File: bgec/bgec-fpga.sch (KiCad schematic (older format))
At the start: 1 part

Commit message: Switch to better FPGA for routing
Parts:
- removed FPGAiCE40HX1: ICE40HX8K-CT256, bgec:BGA256C80P16X16_1400X1400X170, symbol bgec:ICE40HX8K-CT256
- added FPGAiCE40HX1: ICE40HX4K-TQ144, Package_QFP:TQFP-144_20x20mm_P0.5mm, symbol FPGA_Lattice:ICE40HX4K-TQ144
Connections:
- wire segments 65 -> 47
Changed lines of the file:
@@
 Comment4 ""
 $EndDescr
-Text GLabel 2000 1100 0    50   Input ~ 0
+Text GLabel 1500 900  0    50   Input ~ 0
 GCLogic
 Wire Wire Line
-	2000 1100 2100 1100
-Wire Wire Line
-	2100 1100 2100 1200
-Wire Wire Line
-	2100 1100 2200 1100
-Wire Wire Line
-	2200 1100 2200 1200
-Connection ~ 2100 1100
-Wire Wire Line
-	2200 1100 2300 1100
-Wire Wire Line
-	2300 1100 2300 1200
-Connection ~ 2200 1100
-Wire Wire Line
-	2300 1100 2400 1100
-Wire Wire Line
-	2400 1100 2400 1200
-Connection ~ 2300 1100
-Wire Wire Line
-	2400 1100 4100 1100
-Wire Wire Line
-	4100 1100 4100 1200
-Connection ~ 2400 1100
-Wire Wire Line
-	4100 1100 4200 1100
-Wire Wire Line
-	4200 1100 4200 1200
-Connection ~ 4100 1100
-Wire Wire Line
-	4200 1100 4300 1100
-Wire Wire Line
-	4300 1100 4300 1200
-Connection ~ 4200 1100
-Wire Wire Line
-	4300 1100 4400 1100
-Wire Wire Line
-	4400 1100 4400 1200
-Connection ~ 4300 1100
-Wire Wire Line
-	1500 5800 1400 5800
-Wire Wire Line
-	1400 5900 1500 5900
-Wire Wire Line
-	1500 6000 1400 6000
-Wire Wire Line
-	1400 6100 1500 6100
-Wire Wire Line
-	1500 6200 1400 6200
-Wire Wire Line
-	1400 6300 1500 6300
-Wire Wire Line
-	1400 5700 1500 5700
-Wire Wire Line
-	1500 5600 1400 5600
-Wire Wire Line
-	1400 5500 1500 5500
-Wire Wire Line
-	1400 5400 1500 5400
-Wire Wire Line
-	1400 5300 1500 5300
-Wire Wire Line
-	1400 5200 1500 5200
-Wire Wire Line
-	1400 5100 1500 5100
-Wire Wire Line
-	1400 5000 1500 5000
-Wire Wire Line
-	1400 4900 1500 4900
-Wire Wire Line
-	1400 4800 1500 4800
-Wire Wire Line
-	1400 4700 1500 4700
-Wire Wire Line
-	1400 4600 1500 4600
-Wire Wire Line
-	1400 4500 1500 4500
-Wire Wire Line
-	1500 4400 1400 4400
-Wire Wire Line
-	1400 4300 1500 4300
-Wire Wire Line
-	1500 4200 1400 4200
-Wire Wire Line
-	1500 3900 1400 3900
-Wire Wire Line
-	1400 3800 1500 3800
-Wire Wire Line
-	1500 3700 1400 3700
-Wire Wire Line
-	1400 3600 1500 3600
-Wire Wire Line
-	1500 3500 1400 3500
-Wire Wire Line
-	1400 3400 1500 3400
-Text GLabel 1400 6100 0    50   Input ~ 0
+	4000 3900 3900 3900
+Wire Wire Line
+	3900 4000 4000 4000
+Wire Wire Line
+	4000 4100 3900 4100
+Wire Wire Line
+	3900 4200 4000 4200
+Wire Wire Line
+	3900 3800 4000 3800
+Wire Wire Line
+	4000 3700 3900 3700
+Wire Wire Line
+	3900 3600 4000 3600
+Wire Wire Line
+	3900 3500 4000 3500
+Wire Wire Line
+	3900 3400 4000 3400
+Wire Wire Line
+	3900 3300 4000 3300
+Wire Wire Line
+	3900 2400 4000 2400
+Wire Wire Line
+	3900 2300 4000 2300
+Wire Wire Line
+	3900 2200 4000 2200
+Wire Wire Line
+	3900 2100 4000 2100
+Wire Wire Line
+	3900 2000 4000 2000
+Wire Wire Line
+	3900 1900 4000 1900
+Wire Wire Line
+	3900 1800 4000 1800
+Wire Wire Line
+	4000 1700 3900 1700
+Wire Wire Line
+	3900 1600 4000 1600
+Wire Wire Line
+	4000 1500 3900 1500
+Wire Wire Line
+	1500 4000 1400 4000
+Wire Wire Line
+	1400 3900 1500 3900
+Text GLabel 3900 4200 0    50   Input ~ 0
 TriggerRDB0
-Text GLabel 1400 6000 0    50   Input ~ 0
+Text GLabel 3900 4100 0    50   Input ~ 0
 TriggerRDB1
-Text GLabel 1400 5900 0    50   Input ~ 0
+Text GLabel 3900 4000 0    50   Input ~ 0
 TriggerRDB2
-Text GLabel 1400 5800 0    50   Input ~ 0
+Text GLabel 3900 3900 0    50   Input ~ 0
 TriggerRDB3
-Text GLabel 1400 5700 0    50   Input ~ 0
+Text GLabel 3900 3800 0    50   Input ~ 0
 TriggerRDB4
-Text GLabel 1400 5600 0    50   Input ~ 0
+Text GLabel 3900 3700 0    50   Input ~ 0
 TriggerRDB5
-Text GLabel 1400 5500 0    50   Input ~ 0
+Text GLabel 3900 3600 0    50   Input ~ 0
 TriggerRDB6
-Text GLabel 1400 5400 0    50   Input ~ 0
+Text GLabel 3900 3500 0    50   Input ~ 0
 TriggerRDB7
-Text GLabel 1400 5300 0    50   Input ~ 0
+Text GLabel 3900 3400 0    50   Input ~ 0
 TriggerREOC
-Text GLabel 1400 5100 0    50   Input ~ 0
+Text GLabel 3900 2400 0    50   Input ~ 0
 TriggerLDB0
-Text GLabel 1400 5000 0    50   Input ~ 0
+Text GLabel 3900 2300 0    50   Input ~ 0
 TriggerLDB1
-Text GLabel 1400 4900 0    50   Input ~ 0
+Text GLabel 3900 2200 0    50   Input ~ 0
 TriggerLDB2
-Text GLabel 1400 4800 0    50   Input ~ 0
+Text GLabel 3900 2100 0    50   Input ~ 0
 TriggerLDB3
-Text GLabel 1400 4700 0    50   Input ~ 0
+Text GLabel 3900 2000 0    50   Input ~ 0
 TriggerLDB4
-Text GLabel 1400 4600 0    50   Input ~ 0
+Text GLabel 3900 1900 0    50   Input ~ 0
 TriggerLDB5
-Text GLabel 1400 4500 0    50   Input ~ 0
+Text GLabel 3900 1800 0    50   Input ~ 0
 TriggerLDB6
-Text GLabel 1400 4400 0    50   Input ~ 0
+Text GLabel 3900 1700 0    50   Input ~ 0
 TriggerLDB7
-Text GLabel 1400 4300 0    50   Input ~ 0
+Text GLabel 3900 1600 0    50   Input ~ 0
 TriggerLEOC
 Wire Wire Line
@@
 GCData
 Wire Wire Line
+	1400 3800 1500 3800
+Wire Wire Line
+	1400 3700 1500 3700
+Wire Wire Line
+	1400 3600 1500 3600
+Wire Wire Line
+	1400 3500 1500 3500
+Wire Wire Line
+	1400 3400 1500 3400
+Wire Wire Line
 	1400 3300 1500 3300
 Wire Wire Line
@@
 	1400 3100 1500 3100
 Wire Wire Line
-	1400 3000 1500 3000
-Wire Wire Line
-	1400 2900 1500 2900
-Wire Wire Line
-	1400 2800 1500 2800
-Wire Wire Line
-	1400 2700 1500 2700
-Wire Wire Line
-	1400 2600 1500 2600
-Wire Wire Line
 	1400 2500 1500 2500
-Text GLabel 1400 2800 0    50   Input ~ 0
+Text GLabel 1400 3300 0    50   Input ~ 0
 JoystickYDB7
-Text GLabel 1400 2900 0    50   Input ~ 0
+Text GLabel 1400 3400 0    50   Input ~ 0
 JoystickYDB6
-Text GLabel 1400 3000 0    50   Input ~ 0
+Text GLabel 1400 3500 0    50   Input ~ 0
 JoystickYDB5
-Text GLabel 1400 3100 0    50   Input ~ 0
+Text GLabel 1400 3600 0    50   Input ~ 0
 JoystickYDB4
+Text GLabel 1400 3700 0    50   Input ~ 0
+JoystickYDB3
+Text GLabel 1400 3800 0    50   Input ~ 0
+JoystickYDB2
+Text GLabel 1400 3900 0    50   Input ~ 0
+JoystickYDB1
+Text GLabel 1400 4000 0    50   Input ~ 0
+JoystickYDB0
 Text GLabel 1400 3200 0    50   Input ~ 0
-JoystickYDB3
-Text GLabel 1400 3300 0    50   Input ~ 0
-JoystickYDB2
-Text GLabel 1400 3400 0    50   Input ~ 0
-JoystickYDB1
-Text GLabel 1400 3500 0    50   Input ~ 0
-JoystickYDB0
-Text GLabel 1400 2700 0    50   Input ~ 0
 JoystickYEOC
 Wire Wire Line
@@
 JoystickXEOC
 Wire Wire Line
-	1300 4100 1500 4100
-Wire Wire Line
-	1300 4000 1500 4000
-Text GLabel 1300 4000 0    50   Input ~ 0
+	1300 3000 1500 3000
+Wire Wire Line
+	1300 2900 1500 2900
+Text GLabel 1300 2900 0    50   Input ~ 0
 CLK
-Text GLabel 1300 4100 0    50   Input ~ 0
+Text GLabel 1300 3000 0    50   Input ~ 0
 RESET
 $Comp
-L bgec:ICE40HX8K-CT256 FPGAiCE40HX?
-U 2 1 5E7127EF
-P 3500 1500
-AR Path="/5E7127EF" Ref="FPGAiCE40HX?"  Part="2"
-AR Path="/5E6B62E5/5E7127EF" Ref="FPGAiCE40HX1"  Part="2"
-F 0 "FPGAiCE40HX1" H 3900 2100 50  0000 L CNN
-F 1 "ICE40HX8K-CT256" H 3900 2000 50  0000 L CNN
-F 2 "bgec:BGA256C80P16X16_1400X1400X170" H 4750 2500 50  0001 C CNN
-F 3 "http://www.latticesemi.com/Products/FPGAandCPLD/iCE40" H 4600 2400 50  0001 C CNN
-	2    3500 1500
-	1    0    0    -1
-$EndComp
-$Comp
-L bgec:ICE40HX8K-CT256 FPGAiCE40HX?
-U 1 1 5E7127F5
-P 1500 1500
-AR Path="/5E7127F5" Ref="FPGAiCE40HX?"  Part="1"
-AR Path="/5E6B62E5/5E7127F5" Ref="FPGAiCE40HX1"  Part="1"
-F 0 "FPGAiCE40HX1" H 1900 2100 50  0000 L CNN
-F 1 "ICE40HX8K-CT256" H 1900 2000 50  0000 L CNN
-F 2 "bgec:BGA256C80P16X16_1400X1400X170" H 2250 2250 50  0001 C CNN
-F 3 "http://www.latticesemi.com/Products/FPGAandCPLD/iCE40" H 2250 2250 50  0001 C CNN
-	1    1500 1500
-	1    0    0    -1
-$EndComp
+L FPGA_Lattice:ICE40HX4K-TQ144 FPGAiCE40HX1
+U 1 1 5E519664
+P 2000 2700
+F 0 "FPGAiCE40HX1" H 2349 2928 50  0000 L CNN
+F 1 "ICE40HX4K-TQ144" H 2349 2837 50  0000 L CNN
+F 2 "Package_QFP:TQFP-144_20x20mm_P0.5mm" H 3000 800 50  0001 R CNN
+F 3 "http://www.latticesemi.com/Products/FPGAandCPLD/iCE40" H 1000 5200 50  0001 C CNN
+	1    2000 2700
+	1    0    0    -1
+$EndComp
+$Comp
+L FPGA_Lattice:ICE40HX4K-TQ144 FPGAiCE40HX1
+U 2 1 5E5231A3
+P 4500 2800
+F 0 "FPGAiCE40HX1" H 4849 3028 50  0000 L CNN
+F 1 "ICE40HX4K-TQ144" H 4849 2937 50  0000 L CNN
+F 2 "Package_QFP:TQFP-144_20x20mm_P0.5mm" H 5500 900 50  0001 R CNN
+F 3 "http://www.latticesemi.com/Products/FPGAandCPLD/iCE40" H 3500 5300 50  0001 C CNN
+	2    4500 2800
+	1    0    0    -1
+$EndComp
+$Comp
+L FPGA_Lattice:ICE40HX4K-TQ144 FPGAiCE40HX1
+U 3 1 5E52A92F
+P 7000 2300
+F 0 "FPGAiCE40HX1" H 7399 2528 50  0000 L CNN
+F 1 "ICE40HX4K-TQ144" H 7399 2437 50  0000 L CNN
+F 2 "Package_QFP:TQFP-144_20x20mm_P0.5mm" H 8000 400 50  0001 R CNN
+F 3 "http://www.latticesemi.com/Products/FPGAandCPLD/iCE40" H 6000 4800 50  0001 C CNN
+	3    7000 2300
+	1    0    0    -1
+$EndComp
+$Comp
+L FPGA_Lattice:ICE40HX4K-TQ144 FPGAiCE40HX1
+U 4 1 5E52E7E2
+P 9500 2700
+F 0 "FPGAiCE40HX1" H 9849 2878 50  0000 L CNN
+F 1 "ICE40HX4K-TQ144" H 9849 2787 50  0000 L CNN
+F 2 "Package_QFP:TQFP-144_20x20mm_P0.5mm" H 10500 800 50  0001 R CNN
+F 3 "http://www.latticesemi.com/Products/FPGAandCPLD/iCE40" H 8500 5200 50  0001 C CNN
+	4    9500 2700
+	1    0    0    -1
+$EndComp
+$Comp
+L FPGA_Lattice:ICE40HX4K-TQ144 FPGAiCE40HX1
+U 5 1 5E531BCE
+P 2600 6100
+F 0 "FPGAiCE40HX1" H 3344 6146 50  0000 L CNN
+F 1 "ICE40HX4K-TQ144" H 3344 6055 50  0000 L CNN
+F 2 "Package_QFP:TQFP-144_20x20mm_P0.5mm" H 3600 4200 50  0001 R CNN
+F 3 "http://www.latticesemi.com/Products/FPGAandCPLD/iCE40" H 1600 8600 50  0001 C CNN
+	5    2600 6100
+	1    0    0    -1
+$EndComp
+Wire Wire Line
+	1500 900  2000 900
+Wire Wire Line
+	2000 900  4500 900
+Connection ~ 2000 900
+Wire Wire Line
+	4500 900  7000 900
+Connection ~ 4500 900
+Wire Wire Line
+	7000 900  9500 900
+Connection ~ 7000 900
 $EndSCHEMATC

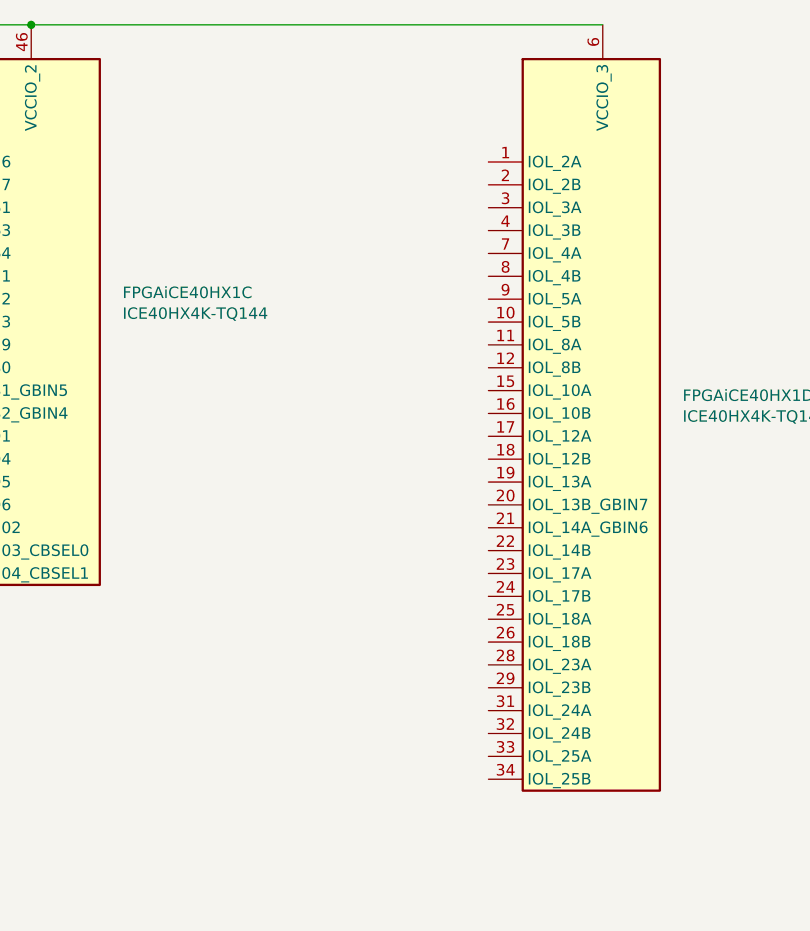
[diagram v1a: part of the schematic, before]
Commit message: Add more ADC connections
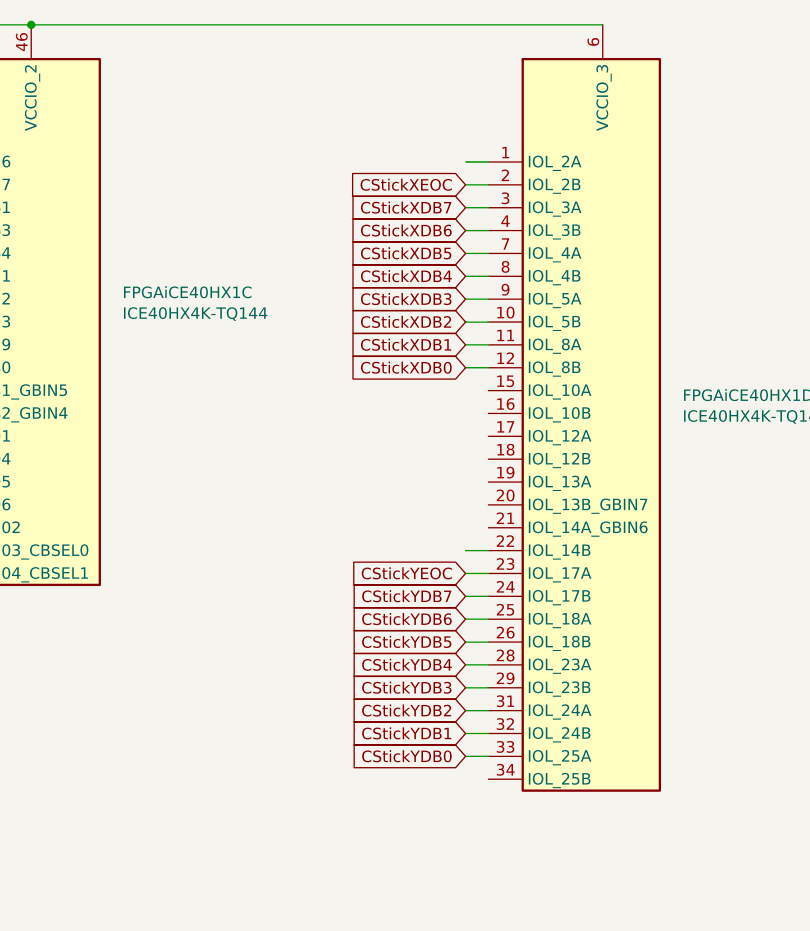
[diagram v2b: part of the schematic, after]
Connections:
- net labels added: CStickXDB0, CStickXDB1, CStickXDB2, CStickXDB3, CStickXDB4, CStickXDB5, CStickXDB6, CStickXDB7, CStickXEOC, CStickYDB0, CStickYDB1, CStickYDB2, CStickYDB3, CStickYDB4, CStickYDB5, CStickYDB6, CStickYDB7, CStickYEOC
- wire segments 47 -> 67
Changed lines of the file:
@@
 	7000 900  9500 900
 Connection ~ 7000 900
+Wire Wire Line
+	8900 2400 9000 2400
+Wire Wire Line
+	8900 2300 9000 2300
+Wire Wire Line
+	8900 2200 9000 2200
+Wire Wire Line
+	8900 2100 9000 2100
+Wire Wire Line
+	8900 2000 9000 2000
+Wire Wire Line
+	8900 1900 9000 1900
+Wire Wire Line
+	8900 1800 9000 1800
+Wire Wire Line
+	9000 1700 8900 1700
+Wire Wire Line
+	8900 1600 9000 1600
+Wire Wire Line
+	9000 1500 8900 1500
+Text GLabel 8900 2400 0    50   Input ~ 0
+CStickXDB0
+Text GLabel 8900 2300 0    50   Input ~ 0
+CStickXDB1
+Text GLabel 8900 2200 0    50   Input ~ 0
+CStickXDB2
+Text GLabel 8900 2100 0    50   Input ~ 0
+CStickXDB3
+Text GLabel 8900 2000 0    50   Input ~ 0
+CStickXDB4
+Text GLabel 8900 1900 0    50   Input ~ 0
+CStickXDB5
+Text GLabel 8900 1800 0    50   Input ~ 0
+CStickXDB6
+Text GLabel 8900 1700 0    50   Input ~ 0
+CStickXDB7
+Text GLabel 8900 1600 0    50   Input ~ 0
+CStickXEOC
+Wire Wire Line
+	8900 4100 9000 4100
+Wire Wire Line
+	8900 4000 9000 4000
+Wire Wire Line
+	8900 3900 9000 3900
+Wire Wire Line
+	8900 3800 9000 3800
+Wire Wire Line
+	8900 3700 9000 3700
+Wire Wire Line
+	8900 3600 9000 3600
+Wire Wire Line
+	8900 3500 9000 3500
+Wire Wire Line
+	9000 3400 8900 3400
+Wire Wire Line
+	8900 3300 9000 3300
+Wire Wire Line
+	9000 3200 8900 3200
+Text GLabel 8900 4100 0    50   Input ~ 0
+CStickYDB0
+Text GLabel 8900 4000 0    50   Input ~ 0
+CStickYDB1
+Text GLabel 8900 3900 0    50   Input ~ 0
+CStickYDB2
+Text GLabel 8900 3800 0    50   Input ~ 0
+CStickYDB3
+Text GLabel 8900 3700 0    50   Input ~ 0
+CStickYDB4
+Text GLabel 8900 3600 0    50   Input ~ 0
+CStickYDB5
+Text GLabel 8900 3500 0    50   Input ~ 0
+CStickYDB6
+Text GLabel 8900 3400 0    50   Input ~ 0
+CStickYDB7
+Text GLabel 8900 3300 0    50   Input ~ 0
+CStickYEOC
 $EndSCHEMATC
